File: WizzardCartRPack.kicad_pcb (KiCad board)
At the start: 2 copper layers, 72.7 x 54.5 mm, 12 parts, among them SW1 SW_DIP_x05, U1 27C801

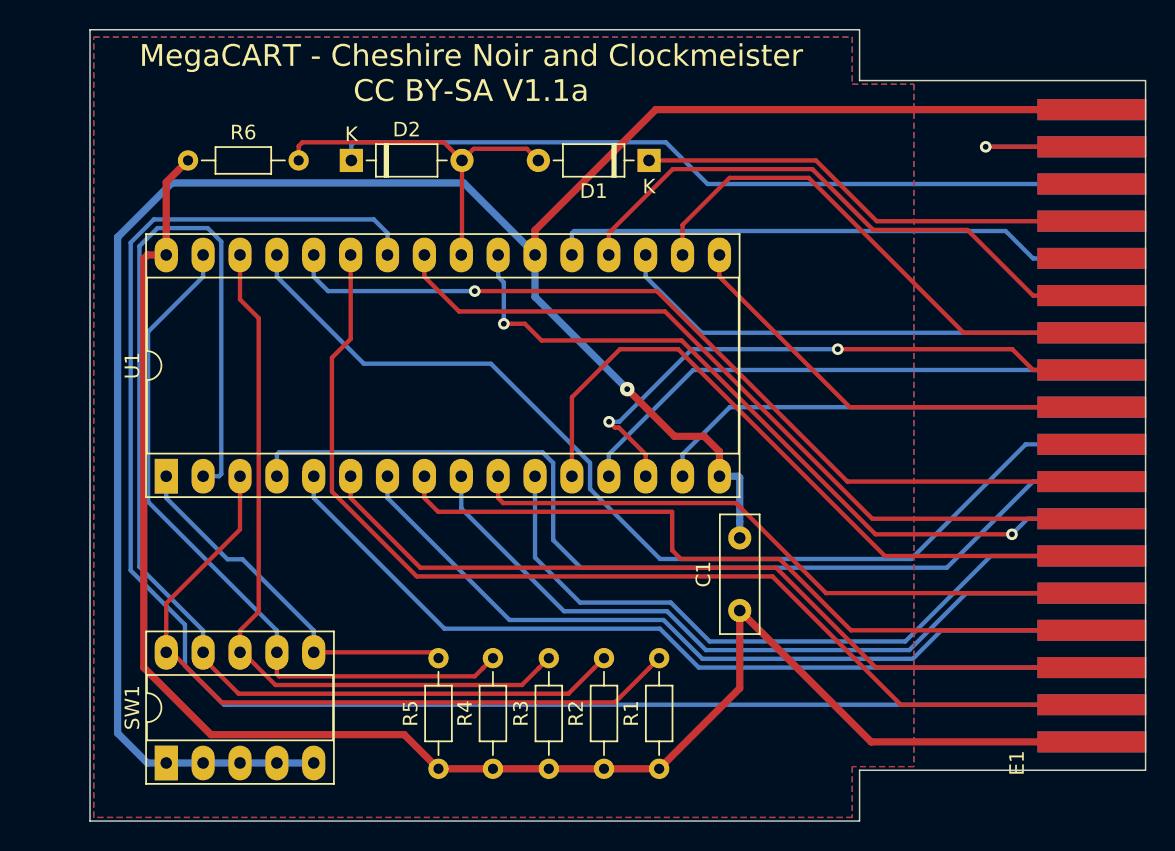
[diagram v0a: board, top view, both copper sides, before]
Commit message: Fabricated single-ROM version
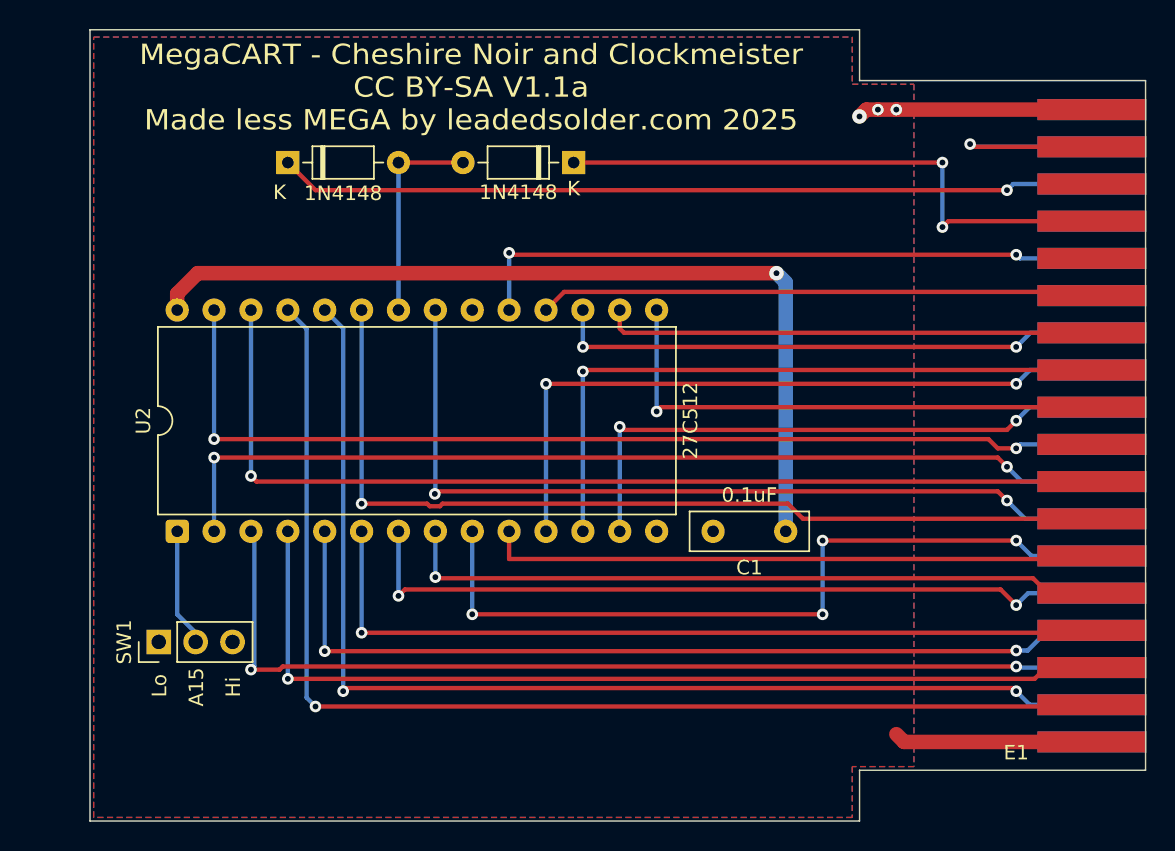
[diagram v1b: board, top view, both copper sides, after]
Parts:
- removed R1, R2, R3, R4, R5, R6: 4.7k, Resistor_THT:R_Axial_DIN0204_L3.6mm_D1.6mm_P7.62mm_Horizontal
- removed U1: 27C801, Package_DIP:DIP-32_W15.24mm_Socket_LongPads
- added U2: 27C512, Package_DIP:DIP-28_W15.24mm, F.Cu at (103.5, 106.0)
- SW1: value SW_DIP_x05 -> SW_SPDT; footprint Package_DIP:DIP-10_W7.62mm_Socket_LongPads -> Connector_PinHeader_2.54mm:PinHeader_1x03_P2.54mm_Vertical
- moved SW1 8.35 mm to (102.2, 113.7)
- moved C1 6.31 mm to (145.4, 106.0), turned to 180 degrees
- moved D1 5.19 mm to (130.8, 80.6)
- moved D2 4.38 mm to (111.1, 80.6)
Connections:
- E1 pad 10: Net-(E1-Pad10) -> /A3
- E1 pad 11: Net-(E1-Pad11) -> /A0
- E1 pad 12: Net-(E1-Pad12) -> /A1
- E1 pad 13: Net-(E1-Pad13) -> /A11
- E1 pad 14: Net-(E1-Pad14) -> /A10
- E1 pad 15: Net-(E1-Pad15) -> /A13
- E1 pad 16: Net-(E1-Pad16) -> /A12
- E1 pad 17: Net-(E1-Pad17) -> unconnected-(E1-A15-Pad17)
- E1 pad 18: Net-(E1-Pad18) -> /A14
- E1 pad 19: Net-(E1-Pad19) -> /D3
- E1 pad 2: Net-(E1-Pad2) -> unconnected-(E1--5v-Pad2)
- E1 pad 20: Net-(E1-Pad20) -> /D2
- E1 pad 21: Net-(E1-Pad21) -> /D1
- E1 pad 22: Net-(E1-Pad22) -> /D0
- E1 pad 23: Net-(E1-Pad23) -> /D4
- E1 pad 24: Net-(E1-Pad24) -> /D5
- E1 pad 25: Net-(E1-Pad25) -> /D6
- E1 pad 26: Net-(E1-Pad26) -> unconnected-(E1-PHI2-Pad26)
- E1 pad 27: Net-(E1-Pad27) -> unconnected-(E1-_RW-Pad27)
- E1 pad 28: Net-(E1-Pad28) -> /D7
- E1 pad 3: Net-(E1-Pad3) -> /A8
- E1 pad 30: Net-(E1-Pad30) -> unconnected-(E1-EAI-Pad30)
- E1 pad 31: Net-(E1-Pad31) -> unconnected-(E1-_RAM-Pad31)
- E1 pad 36: Net-(E1-Pad36) -> unconnected-(E1-+12v-Pad36)
- E1 pad 4: Net-(E1-Pad4) -> /A9
- E1 pad 5: Net-(E1-Pad5) -> /A6
- E1 pad 6: Net-(E1-Pad6) -> /A7
- E1 pad 7: Net-(E1-Pad7) -> /A4
- E1 pad 8: Net-(E1-Pad8) -> /A5
- E1 pad 9: Net-(E1-Pad9) -> /A2
- SW1 pad 2: GND -> Net-(SW1-B)
- SW1 pad 3: GND -> +5V
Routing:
- net GND: track 151.7 -> 16.2 mm, vias 1 -> 3
- net Net-(E1-Pad4): track 114.5 -> 0.00 mm
- net Net-(R2-Pad2): track 83.7 -> 0.00 mm
- net /A8: track 0.00 -> 81.6 mm, vias 0 -> 1
- net /A9: track 0.00 -> 78.9 mm, vias 0 -> 2
- net Net-(E1-Pad3): track 75.3 -> 0.00 mm
- net Net-(E1-Pad18): track 70.0 -> 0.00 mm
- net /A14: track 0.00 -> 69.7 mm, vias 0 -> 2
- net /A13: track 0.00 -> 69.5 mm, vias 0 -> 1
- net /A7: track 0.00 -> 67.8 mm, vias 0 -> 2
- net Net-(E1-Pad16): track 66.6 -> 0.00 mm
- net /A12: track 0.00 -> 66.2 mm, vias 0 -> 2
- net /A6: track 0.00 -> 65.9 mm, vias 0 -> 1
- net /A11: track 0.00 -> 64.2 mm, vias 0 -> 1
- net /A5: track 0.00 -> 61.7 mm, vias 0 -> 2
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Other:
- rule pad_to_mask_clearance: 0.051 -> 0
- board text added: "A15"
- board text added: "Hi"
- board text added: "Lo"
- board text added: "MegaCART - Cheshire Noir and Clockmeister CC BY-SA V1.1a Made less MEGA by leadedsolder.com 2025"
- board text removed: "MegaCART - Cheshire Noir and Clockmeister CC BY-SA V1.1a"

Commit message: Move fingers up
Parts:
- moved E1 0.76 mm to (159.7, 120.5)
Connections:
- net Net-(D1-A) renamed /~{OE}
- net Net-(D1-K) renamed /~{ROM1}
- net Net-(D2-K) renamed /~{ROM2}
- net Net-(SW1-B) renamed /A15
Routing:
- net /A6: track 65.9 -> 68.3 mm
- net /A5: track 61.7 -> 63.9 mm
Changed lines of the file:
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@@
 	(net 1 "GND")
 	(net 2 "+5V")
-	(net 3 "Net-(D1-K)")
-	(net 4 "Net-(D1-A)")
-	(net 5 "Net-(D2-K)")
+	(net 3 "/~{ROM1}")
+	(net 4 "/~{OE}")
+	(net 5 "/~{ROM2}")
 	(net 6 "/A1")
 	(net 7 "/A10")
@@
 	(net 35 "/A7")
 	(net 36 "unconnected-(E1-PHI2-Pad26)")
-	(net 37 "Net-(SW1-B)")
+	(net 37 "/A15")
 	(footprint "Diode_THT:D_DO-35_SOD27_P7.62mm_Horizontal"
 		(layer "F.Cu")
@@
 			(layers "*.Cu" "*.Mask")
 			(remove_unused_layers no)
-			(net 5 "Net-(D2-K)")
+			(net 5 "/~{ROM2}")
 			(pinfunction "K")
 			(pintype "passive")
@@
 			(layers "*.Cu" "*.Mask")
 			(remove_unused_layers no)
-			(net 4 "Net-(D1-A)")
+			(net 4 "/~{OE}")
 			(pinfunction "A")
 			(pintype "passive")
@@
 	(footprint "WizzardCart:36Edge"
 		(layer "F.Cu")
-		(at 160.5 120.55 90)
+		(at 159.735 120.55 90)
 		(property "Reference" "E1"
 			(at -0.735 0.79 180)
 			(layer "F.SilkS")
+			(hide yes)
 			(effects
 				(font
@@
 			(size 1.45 7.5)
 			(layers "F.Cu" "F.Mask")
-			(net 3 "Net-(D1-K)")
+			(net 3 "/~{ROM1}")
 			(pinfunction "_ROM1")
 			(pintype "bidirectional")
@@
 			(size 1.45 7.5)
 			(layers "B.Cu" "B.Mask")
-			(net 5 "Net-(D2-K)")
+			(net 5 "/~{ROM2}")
 			(pinfunction "_ROM2")
 			(pintype "bidirectional")
@@
 			(layers "*.Cu" "*.Mask")
 			(remove_unused_layers no)
-			(net 3 "Net-(D1-K)")
+			(net 3 "/~{ROM1}")
 			(pinfunction "K")
 			(pintype "passive")
@@
 			(layers "*.Cu" "*.Mask")
 			(remove_unused_layers no)
-			(net 4 "Net-(D1-A)")
+			(net 4 "/~{OE}")
 			(pinfunction "A")
 			(pintype "passive")
@@
 			(layers "*.Cu" "*.Mask")
 			(remove_unused_layers no)
-			(net 37 "Net-(SW1-B)")
+			(net 37 "/A15")
 			(pinfunction "B")
 			(pintype "passive")
@@
 			(remove_unused_layers no)
 			(roundrect_rratio 0.15625)
-			(net 37 "Net-(SW1-B)")
+			(net 37 "/A15")
 			(pinfunction "A15")
 			(pintype "input")
@@
 			(layers "*.Cu" "*.Mask")
 			(remove_unused_layers no)
-			(net 4 "Net-(D1-A)")
+			(net 4 "/~{OE}")
 			(pinfunction "~{OE}")
 			(pintype "input")
@@
 	)
 	(segment
-		(start 161.29 86.995)
+		(start 160.655 86.995)
 		(end 126.495 86.995)
 		(width 0.3)
@@
 	)
 	(via
-		(at 161.29 86.995)
+		(at 160.655 86.995)
 		(size 0.8)
 		(drill 0.4)
@@
 	)
 	(segment
-		(start 161.542068 87.247068)
-		(end 161.29 86.995)
+		(start 126.365 90.805)
+		(end 126.365 86.865)
 		(width 0.3)
 		(layer "B.Cu")
@@
 	)
 	(segment
-		(start 126.365 90.805)
-		(end 126.365 86.865)
+		(start 160.655 86.995)
+		(end 161.542068 87.247068)
 		(width 0.3)
 		(layer "B.Cu")
@@
 	)
 	(segment
-		(start 166.5 87.247068)
-		(end 161.542068 87.247068)
+		(start 161.542068 87.247068)
+		(end 166.5 87.247068)
 		(width 0.3)
 		(layer "B.Cu")
@@
 		(net 13)
 	)
-	(segment
-		(start 166.5 112.864708)
-		(end 166.334708 113.03)
-		(width 0.3)
-		(layer "F.Cu")
-		(net 13)
-	)
 	(via
 		(at 116.205 113.03)
@@
 	)
 	(segment
-		(start 166.5 89.808832)
-		(end 166.245168 89.554)
-		(width 0.3)
-		(layer "F.Cu")
-		(net 14)
-	)
-	(segment
 		(start 130.156 89.554)
 		(end 128.905 90.805)
@@
 	)
 	(segment
-		(start 163.475 112.864708)
-		(end 162.084711 114.254997)
+		(start 162.680289 112.864708)
+		(end 165.735 112.864708)
 		(width 0.3)
 		(layer "B.Cu")
@@
 	)
 	(segment
-		(start 162.084711 114.254997)
-		(end 161.29 114.254997)
+		(start 161.29 114.254997)
+		(end 162.680289 112.864708)
 		(width 0.3)
 		(layer "B.Cu")
@@
 	)
 	(segment
-		(start 161.29 111.125)
-		(end 160.214 110.049)
+		(start 160.214 110.049)
+		(end 119.186 110.049)
 		(width 0.3)
 		(layer "F.Cu")
@@
 	)
 	(segment
-		(start 119.186 110.049)
-		(end 118.745 110.49)
+		(start 160.9725 110.8075)
+		(end 160.214 110.049)
 		(width 0.3)
 		(layer "F.Cu")
@@
 	)
 	(segment
-		(start 160.214 110.049)
-		(end 119.186 110.049)
+		(start 119.186 110.049)
+		(end 118.745 110.49)
 		(width 0.3)
 		(layer "F.Cu")
@@
 	)
 	(via
-		(at 161.29 111.125)
+		(at 160.9725 110.8075)
 		(size 0.8)
 		(drill 0.4)
@@
 	)
 	(segment
-		(start 166.5 110.302944)
-		(end 162.112056 110.302944)
+		(start 162.112056 110.302944)
+		(end 166.5 110.302944)
 		(width 0.3)
 		(layer "B.Cu")
@@
 	)
 	(segment
-		(start 162.112056 110.302944)
-		(end 161.29 111.125)
+		(start 160.9725 110.8075)
+		(end 162.112056 110.302944)
 		(width 0.3)
 		(layer "B.Cu")
@@
 		(net 23)
 	)
-	(segment
-		(start 166.5 117.988236)
-		(end 166.378236 118.11)
-		(width 0.3)
-		(layer "F.Cu")
-		(net 23)
-	)
 	(via
 		(at 113.03 118.11)
@@
 	)
 	(segment
-		(start 160.02 100.33)
-		(end 159.385 99.695)
+		(start 159.385 99.695)
+		(end 106.045 99.695)
 		(width 0.3)
 		(layer "F.Cu")
@@
 	)
 	(segment
-		(start 161.29 100.33)
-		(end 160.02 100.33)
+		(start 160.02 100.33)
+		(end 159.385 99.695)
 		(width 0.3)
 		(layer "F.Cu")
@@
 	)
 	(segment
-		(start 159.385 99.695)
-		(end 106.045 99.695)
+		(start 160.655 100.33)
+		(end 160.02 100.33)
 		(width 0.3)
 		(layer "F.Cu")
@@
 	)
 	(via
-		(at 161.29 100.33)
+		(at 160.655 100.33)
 		(size 0.8)
 		(drill 0.4)
@@
 	)
 	(segment
-		(start 161.564112 100.055888)
-		(end 161.29 100.33)
+		(start 160.655 100.33)
+		(end 161.564112 100.055888)
 		(width 0.3)
 		(layer "B.Cu")
@@
 	)
 	(segment
-		(start 166.5 100.055888)
-		(end 161.564112 100.055888)
+		(start 106.045 99.695)
+		(end 106.045 90.805)
 		(width 0.3)
 		(layer "B.Cu")
@@
 	)
 	(segment
-		(start 106.045 99.695)
-		(end 106.045 90.805)
+		(start 161.564112 100.055888)
+		(end 166.5 100.055888)
 		(width 0.3)
 		(layer "B.Cu")
@@
 	)
 	(segment
-		(start 163.338528 115.426472)
-		(end 162.56 116.205)
+		(start 162.703528 115.426472)
+		(end 161.925 116.205)
+		(width 0.3)
+		(layer "F.Cu")
+		(net 31)
+	)
+	(segment
+		(start 161.925 116.205)
+		(end 111.125 116.205)
 		(width 0.3)
 		(layer "F.Cu")
@@
 	)
 	(segment
-		(start 162.56 116.205)
-		(end 111.125 116.205)
+		(start 165.735 115.426472)
+		(end 162.703528 115.426472)
 		(width 0.3)
 		(layer "F.Cu")
@@
 	)
 	(segment
-		(start 166.5 107.74118)
-		(end 166.29118 107.95)
-		(width 0.3)
-		(layer "F.Cu")
-		(net 33)
-	)
-	(segment
 		(start 166.29118 107.95)
 		(end 126.365 107.95)
@@
 	)
 	(segment
-		(start 110.557918 115.57)
+		(start 160.655 115.355)
 		(end 110.772918 115.355)
 		(width 0.3)
@@
 	(segment
 		(start 110.772918 115.355)
-		(end 161.29 115.355)
+		(end 110.557918 115.57)
 		(width 0.3)
 		(layer "F.Cu")
@@
 	)
 	(segment
-		(start 108.585 115.57)
-		(end 110.557918 115.57)
+		(start 110.557918 115.57)
+		(end 108.585 115.57)
 		(width 0.3)
 		(layer "F.Cu")
@@
 	)
 	(via
-		(at 161.29 115.355)
+		(at 160.655 115.355)
 		(size 0.8)
 		(drill 0.4)
@@
 	)
 	(segment
-		(start 166.5 115.426472)
+		(start 160.655 115.355)
 		(end 161.361472 115.426472)
 		(width 0.3)
@@
 	(segment
 		(start 161.361472 115.426472)
-		(end 161.29 115.355)
+		(end 166.5 115.426472)
 		(width 0.3)
 		(layer "B.Cu")
